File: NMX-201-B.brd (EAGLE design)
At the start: 50.8 x 50.2 mm, 61 parts, among them IC1 A4983TOP, IC2 A4983TOP, IC3 A4983TOP, J1 MOLEX-4-RAPRO-CONNECTOR, J2 MOLEX-4-RAPRO-CONNECTOR, J3 MOLEX-4-RAPRO-CONNECTOR, U1 CADJ, U2 CADJ, U3 MOUNT-HOLE3.2, U4 MOUNT-HOLE3.2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

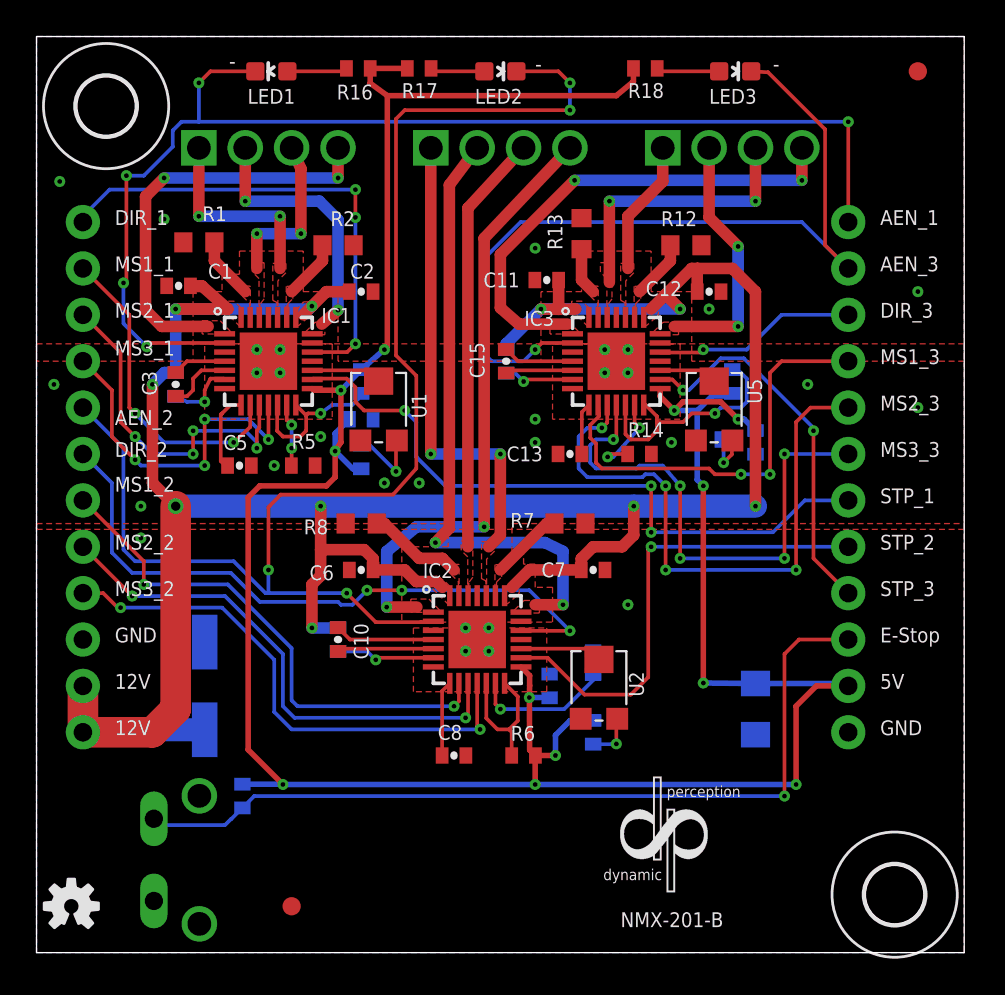
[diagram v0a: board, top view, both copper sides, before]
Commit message: Added DIP switches and increased LED resistor vals
NMX 201-B:
- Added switches to allow users to turn off motor movement indicator
LEDs.
- Changed R16, R17, R19 to 14k resistances in order to reduce LED
brightness.
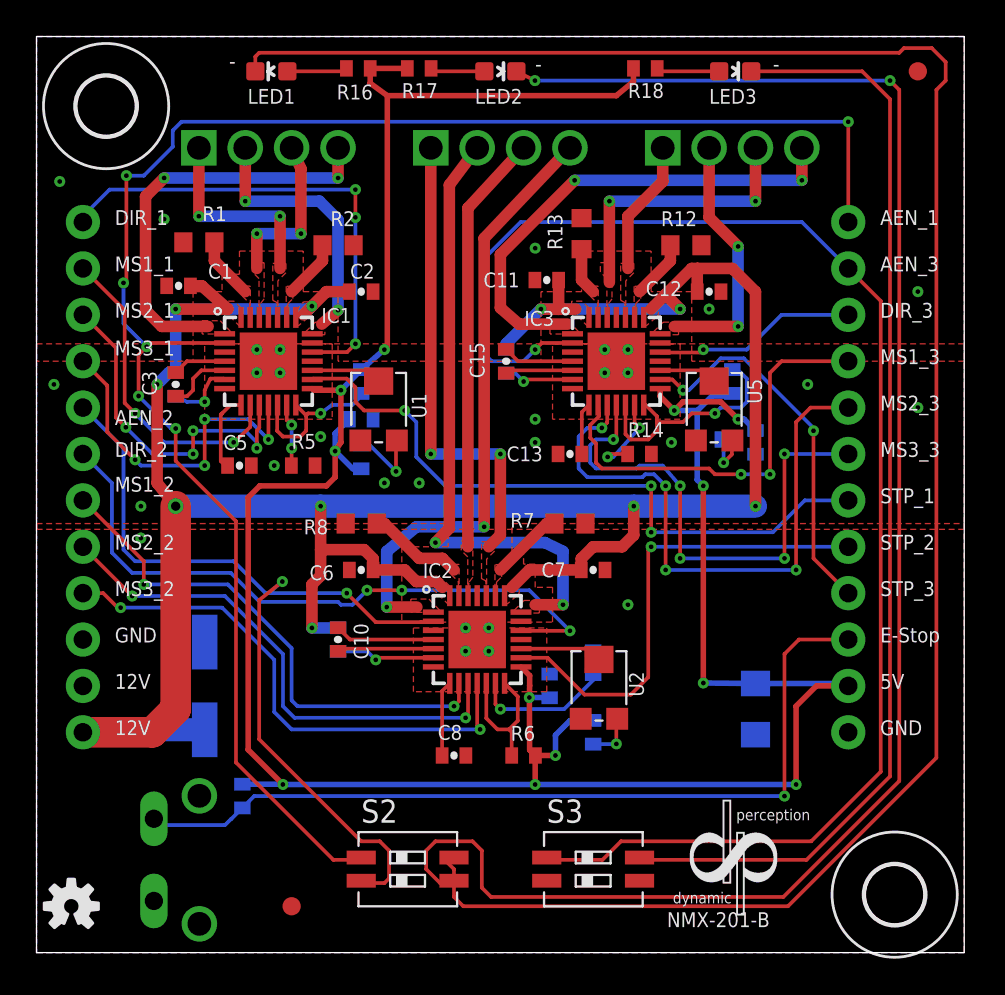
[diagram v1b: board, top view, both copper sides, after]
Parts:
- added S2, S3: CHS-02A, switch-copal:CHS-02A
- R16, R17, R18: value 430 -> 14k
- moved U$1 4.02 mm to (38.1, 5.08)
- moved FRAME2 2.54 mm to (34.5, 1.40)
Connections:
- new net N$16: LED1.C, S2.4
- new net N$18: LED2.C, S2.3
- new net N$19: LED3.C, S3.4
- net AEN_1: now also S2.1; no longer LED1.C
- net AEN_2: now also S2.2; no longer LED2.C
- net AEN_3: now also S3.1; no longer LED3.C
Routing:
- net N$16: track 0.00 -> 110.2 mm
- net N$18: track 0.00 -> 93.2 mm, vias 0 -> 2
- net N$19: track 0.00 -> 61.0 mm
- net AEN_3: track 45.9 -> 81.0 mm
- net AEN_1: track 66.6 -> 95.5 mm, vias 5 -> 6
- net AEN_2: track 75.1 -> 50.7 mm, vias 4 -> 2
- net 12V: track 147.4 -> 144.4 mm
